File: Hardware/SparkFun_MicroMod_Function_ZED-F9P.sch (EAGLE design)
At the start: 51 parts, among them J2 MICROMOD_STANDARD, J3 QWIIC_RA, U1 EEPROM, U2 PCA9306DCUR, U3 U-BLOX_ZED-F9P, U4 74LVC541ABQ, U5 74LVC541ABQ, U6 SN74AUP1T04DCK

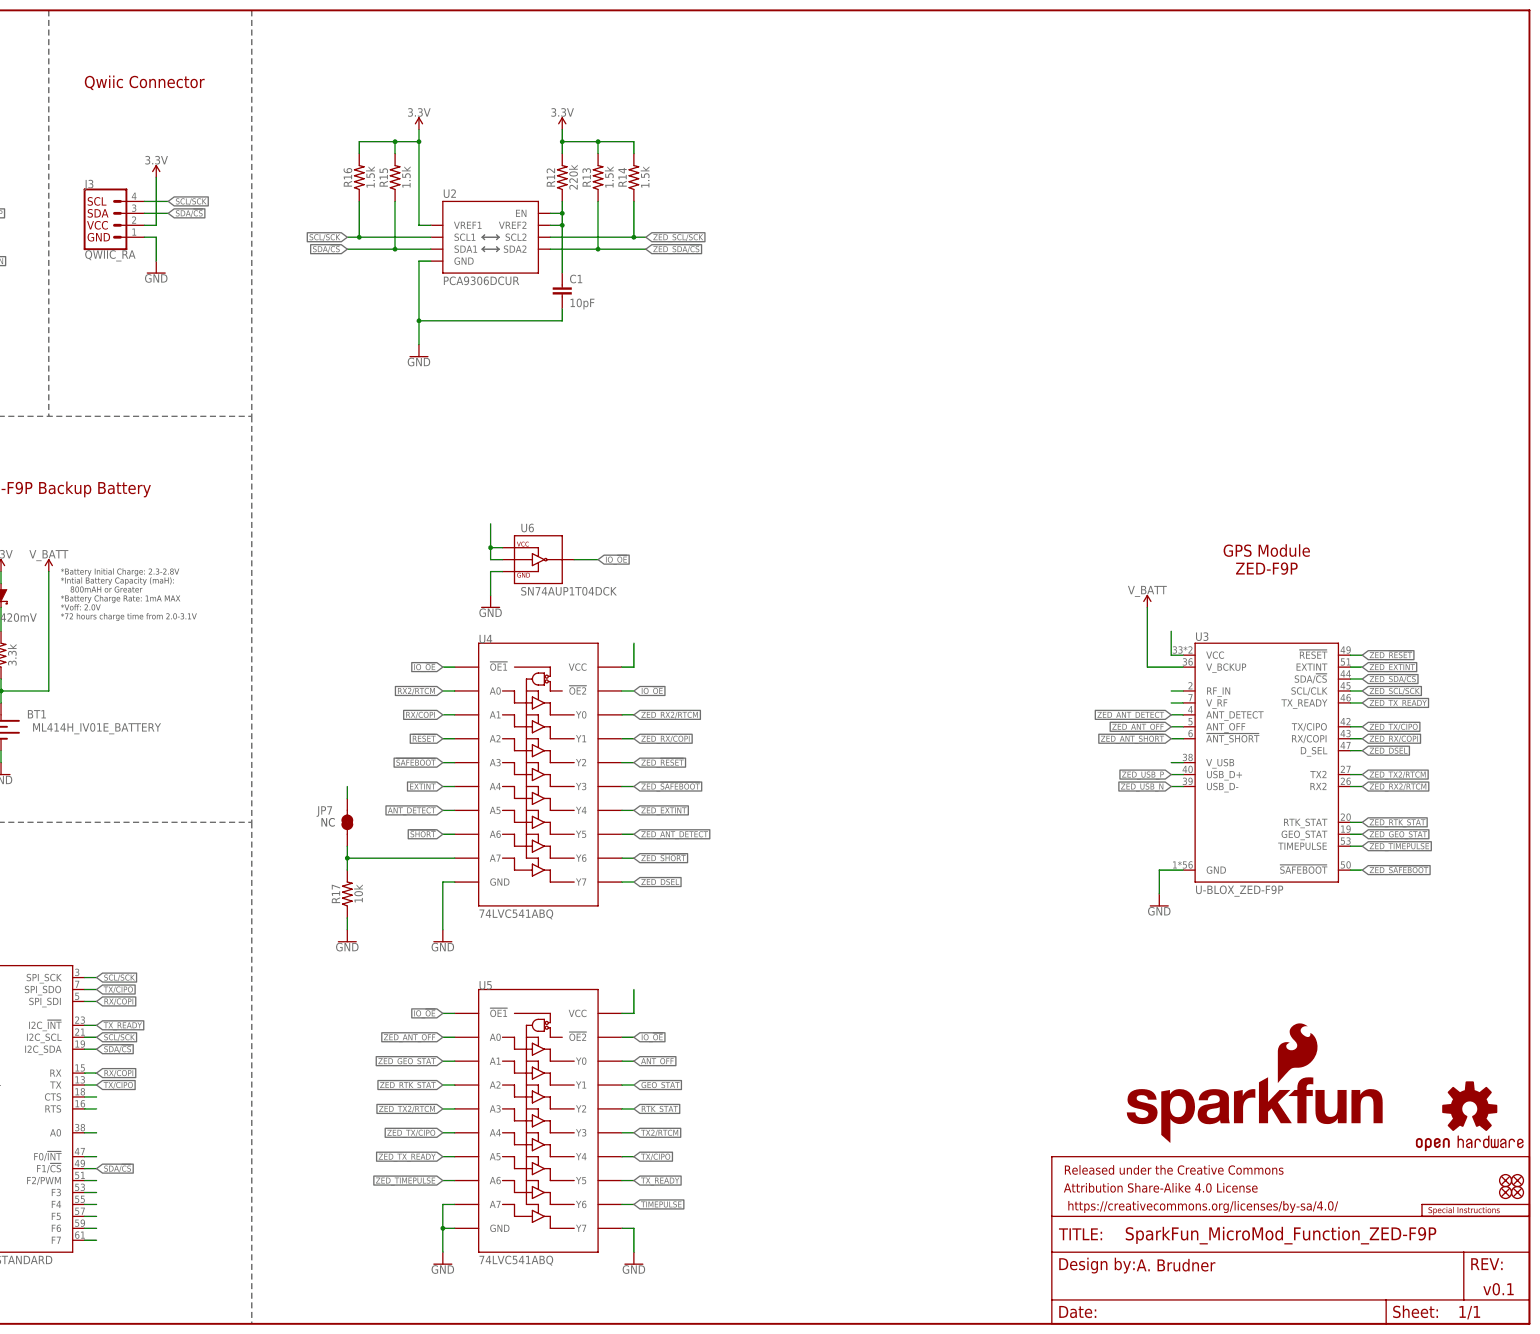
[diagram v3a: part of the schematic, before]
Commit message: Added I/O and passives. Changed net names.
Added passives surrounding IC's.
Modified names to be more descriptive.
Reorganized schematic for visual representation.
Added Descriptions of schematic symbols.
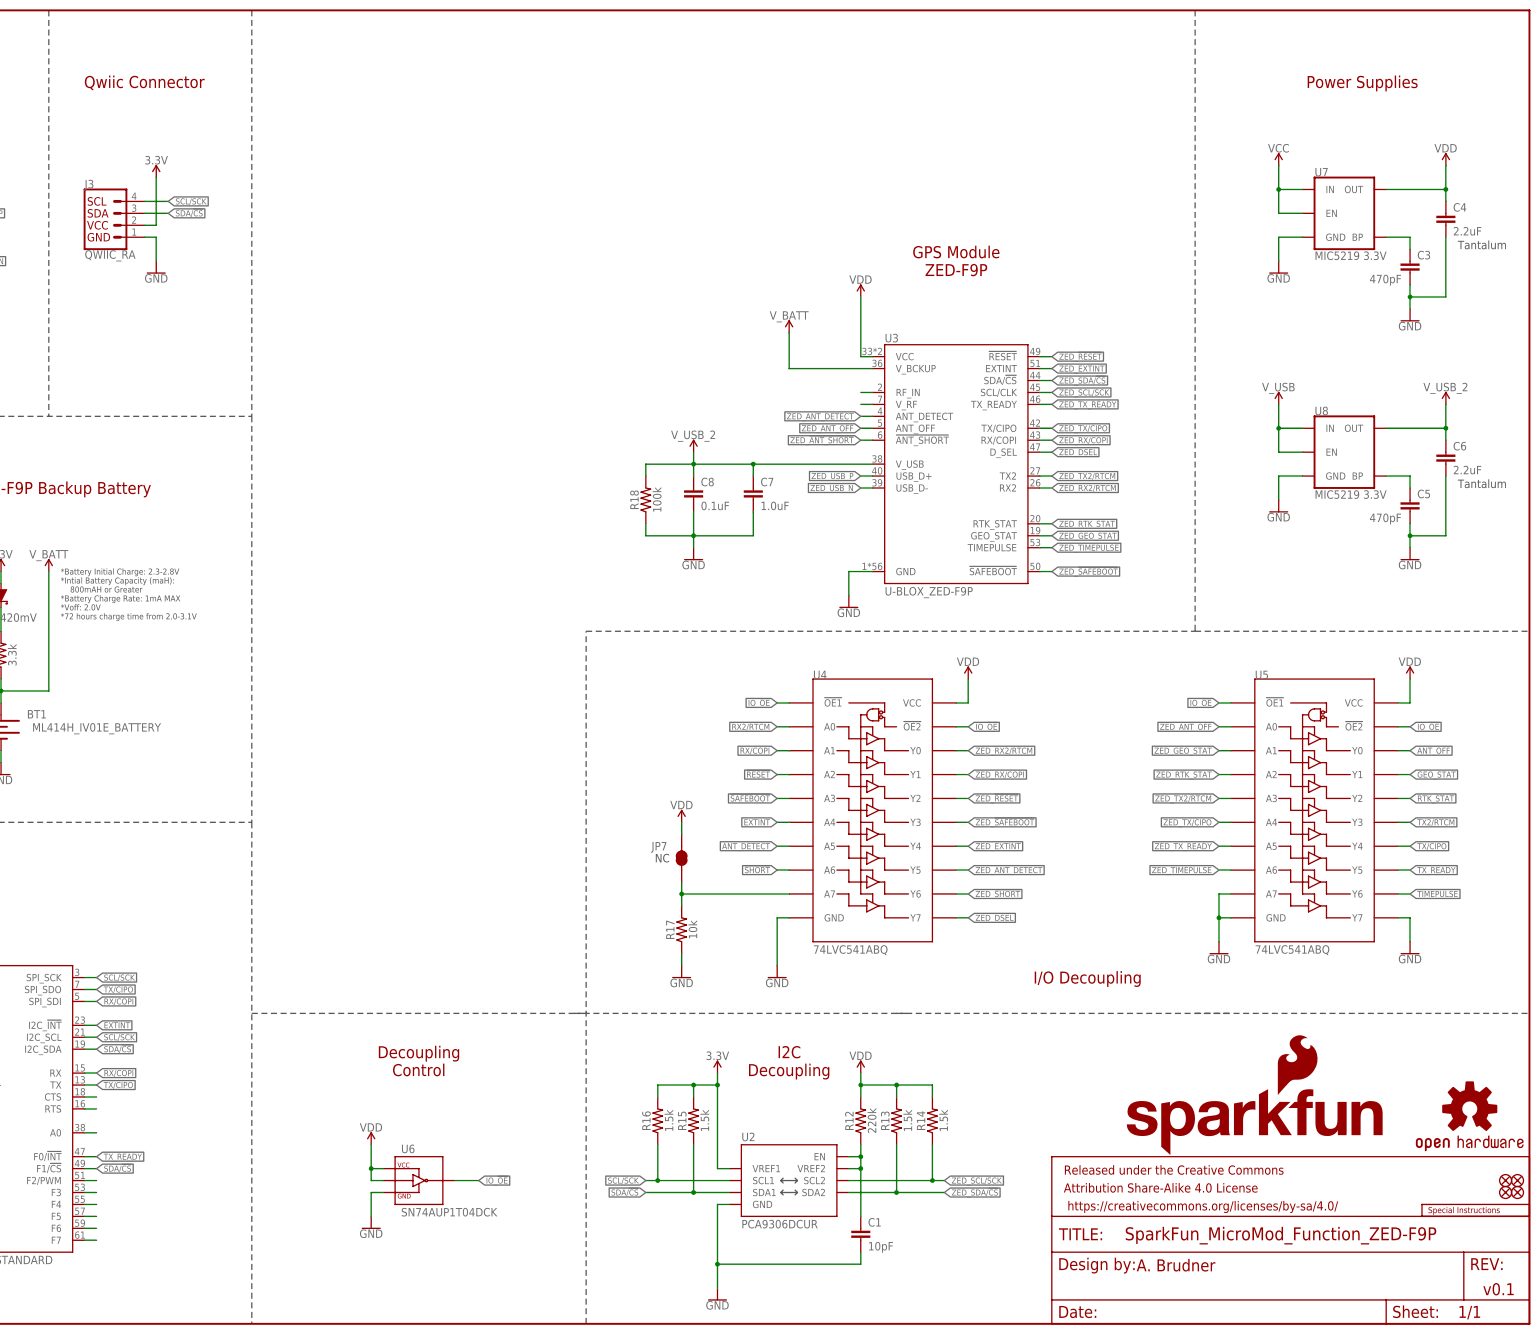
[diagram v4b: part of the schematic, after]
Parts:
- added C3, C5: 470pF, SparkFun-Capacitors:470PF-0603-50V-5%
- added C4, C6: 2.2uF, SparkFun-Capacitors:2.2UF-0603-10V-20%
- added C7: 1.0uF, SparkFun-Capacitors:1.0UF-0603-16V-10%
- added C8: 0.1uF, SparkFun-Capacitors:0.1UF-0402T-16V-10%
- added R18: 100k, SparkFun-Resistors:100KOHM-0603-1/10W-1%
- added U7, U8: MIC5219 3.3V, SparkFun-IC-Power:V_REG_MIC52193.3V
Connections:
- removed net N$16: JP7.2
- removed net N$19: J2.F0/!INT!
- removed net N$39: U4.VCC
- removed net N$42: U5.VCC
- removed net N$69: U3.V_USB
- removed net N$77: U3.VCC
- new net N$17: C3.1, U7.BP
- new net VDD: C4.1, JP7.2, R12.2, R13.2, R14.2, U3.VCC, U4.VCC, U5.VCC, U6.A, U6.VCC, U7.OUT
- new net V_USB_2: C6.1, C7.1, C8.1, R18.2, U3.V_USB, U8.OUT
- net 3.3V: no longer R12.2, R13.2, R14.2
- net EXTINT: now also J2.I2C_!INT!
- net GND: now also C3.2, C4.2, C5.2, C6.2, C7.2, C8.2, R18.1, U7.GND, U8.GND
- net N$14: now also C5.1, U8.BP; no longer U6.A, U6.VCC
- net TX_READY: now also J2.F0/!INT!; no longer J2.I2C_!INT!
- net VCC: now also U7.EN, U7.IN
- net V_USB: now also U8.EN, U8.IN
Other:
- note added: "Decoupling Control"
- note added: "I/O Decoupling"
- note added: "I2C Decoupling"
- note added: "Power Supplies"
- note added: "Tantalum"
- moved on the sheet: C1, JP7, R12, R13, R14, R15, R16, R17, U2, U3, U4, U5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

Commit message: Completed antenna supervisor. Started External Antenna Power.
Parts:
- removed U3: U-BLOX_ZED-F9P, MicroMod_Function_GNSS_ublox_ZED-F9P:U-BLOX_ZED-F9P
- added BYP, USB_EN: JUMPER-SMT_2_NO_SILK, SparkFun-Jumpers:JUMPER-SMT_2_NO_SILK
- added C10, C11, C14: 0.1uF, SparkFun-Capacitors:0.1UF-0402-16V-10%
- added C12: GRM0335C1H470JA01, MicroMod_Function_GNSS_ublox_ZED_F9P:GRM0335C1H470JA01
- added C13: 10nF, SparkFun-Capacitors:10NF-0402T-25V-10%-X7R-WE
- added C9: 0402YD104JAT2A, MicroMod_Function_GNSS_ublox_ZED_F9P:0402YD104JAT2A
- added D10, D9: 3A/10V/280mV, SparkFun-DiscreteSemi:DIODE-SCHOTTKY-BAT60A
- added D11, D12, D8: RED, SparkFun-LED:LED-RED0603
- added D13: PESD0402, SparkFun-DiscreteSemi:PESD0402
- added F1: 6V/2A, SparkFun-Fuses:PPTC_6V2A
- added FB1: BLM18AG102BH1D, MicroMod_Function_GNSS_ublox_ZED_F9P:BLM18AG102BH1D
- added J4: U.FL, SparkFun-RF:ANTENNA-SMA-GROUNDEDEDGE_SMA
- added JP10, JP8, JP9: JUMPER-SMT_2_NC_TRACE_SILK, SparkFun-Jumpers:JUMPER-SMT_2_NC_TRACE_SILK
- added JP11, JP12: JUMPER-SMT_3_2-NC_TRACE_SILK, SparkFun-Jumpers:JUMPER-SMT_3_2-NC_TRACE_SILK
- added L1, L2: LQW15ANR12J00D, MicroMod_Function_GNSS_ublox_ZED_F9P:LQW15ANR12J00D
- added Q1: DMP21D0UT, MicroMod_Function_GNSS_ublox_ZED_F9P:DMP21D0UT
- added Q2, Q3: 600mA/40V, SparkFun-DiscreteSemi:TRANS_PNP-MMBT4403
- added R19, R20, R21, R23: 1k, SparkFun-Resistors:1KOHM-0603-1/10W-1%
- added R22, R26: CRGP2010F10R, MicroMod_Function_GNSS_ublox_ZED_F9P:CRGP2010F10R
- added R24, R25: 100k, SparkFun-Resistors:100KOHM-0603-1/10W-1%
- added R27: 220, SparkFun-Resistors:220OHM-0603-1/10W-1%
- added R28: 2.2k, SparkFun-Resistors:2.2KOHM-0603-1/10W-1%
- added U$3: OPA344, SparkFun-IC-Amplifiers:OPA344
- added U9: 74LVC541ABQ, MicroMod_Function_GNSS_ublox_ZED_F9P:74LVC541ABQ
- JP7: value NC -> JUMPER-SMT_2_NO_SILK; device SparkFun-Jumpers:JUMPER-SMT_2_NC_TRACE_SILK -> SparkFun-Jumpers:JUMPER-SMT_2_NO_SILK
- R17: value 10k -> 100k; device SparkFun-Resistors:10KOHM-0603-1/10W-1% -> SparkFun-Resistors:100KOHM-0603-1/10W-1%
- U2: value PCA9306DCUR -> U-BLOX_ZED-F9P; device MicroMod_Function_GNSS_ublox_ZED-F9P:PCA9306DCUR -> MicroMod_Function_GNSS_ublox_ZED_F9P:U-BLOX_ZED-F9P
- U4: value 74LVC541ABQ -> SN74AUP1T04DCK; device MicroMod_Function_GNSS_ublox_ZED-F9P:74LVC541ABQ -> MicroMod_Function_GNSS_ublox_ZED_F9P:SN74AUP1T04DCK
- U5: value 74LVC541ABQ -> PCA9306DCUR; device MicroMod_Function_GNSS_ublox_ZED-F9P:74LVC541ABQ -> MicroMod_Function_GNSS_ublox_ZED_F9P:PCA9306DCUR
- U6: value SN74AUP1T04DCK -> 74LVC541ABQ; device MicroMod_Function_GNSS_ublox_ZED-F9P:SN74AUP1T04DCK -> MicroMod_Function_GNSS_ublox_ZED_F9P:74LVC541ABQ
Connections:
- removed net !SHORT!: U4.A6
- removed net N$73: U3.V_RF
- removed net N$74: U3.RF_IN
- removed net TIMEPULSE: U5.Y6
- removed net ZED_!ANT_SHORT!: U3.!ANT_SHORT!
- removed net ZED_!SHORT!: U4.Y6
- removed net ZED_TIMEPULSE: U3.TIMEPULSE, U5.A6
- new net ANT_!SHORT!: Q1.D, R22.2, R23.2, U6.A6
- new net GND2: JP10.2, JP2.2, JP3.2, JP4.1, JP5.1, JP6.1, JP8.2, JP9.2
- new net GND_RF: C13.2, C14.1, C3.2, C4.2, C5.2, C6.2, C7.2, C8.2, C9.2, D13.1, J4.GND, R18.1, R24.1, R28.1, U$3G2.P$V-, U2.GND
- new net N$15: JP8.1, R19.1
- new net N$16: D8.C, R19.2
- new net N$19: D10.A, USB_EN.2
- new net N$20: BYP.1, D10.C, D9.C, F1.1
- new net N$39: JP10.1, R21.1
- new net N$40: D12.C, R21.2
- new net N$41: C9.1, L2.2, Q3.C
- new net N$42: JP12.1, R14.2
- new net N$43: JP11.1, R15.2
- new net N$44: JP11.3, R16.2
- new net N$47: JP12.3, R13.2
- new net N$48: R23.1, R24.2, U$3G1.+IN
- new net N$49: C13.1, L1.2, R22.1, U$3G1.-IN
- new net N$50: Q2.B, Q3.E, R26.1
- new net N$51: Q2.C, Q3.B, R28.2
- new net N$52: Q2.E, R27.1
- new net N$53: FB1.2, R26.2, R27.2
- new net RF_IN: C12.2, U2.RF_IN
- new net SMA_RF_IN: C12.1, D13.2, J4.SIGNAL, L1.1, L2.1
- new net V_RF: C14.2, Q1.S, R25.1, U$3G2.P$V+, U2.V_RF
- new net ZED_ANT_!SHORT!: U2.!ANT_SHORT!, U6.Y6
- new net ZED_PPS: U2.TIMEPULSE, U9.A6
- net !RESET!: now also U6.A2; no longer U4.A2
- net !SAFEBOOT!: now also U6.A3; no longer U4.A3
- net 3.3V: now also JP11.2, U5.VREF1; no longer R15.2, R16.2, U2.VREF1
- net ANT_DETECT: now also U$3G1.OUT, U6.A5; no longer U4.A5
- net ANT_OFF: now also Q1.G, R25.2, U9.Y0; no longer U5.Y0
- net EXTINT: now also U6.A4; no longer U4.A4
- net GEO_STAT: now also U9.Y1; no longer U5.Y1
- net GND: now also C10.2, C11.2, JP7.1, U9.A7, U9.GND, U9.Y7; no longer C3.2, C4.2, C5.2, C6.2, C7.2, C8.2, JP2.2, JP3.2, JP4.1, JP5.1, JP6.1, R17.1, R18.1, U2.GND, U3.GND, U5.A7, U5.Y7
- net IO_!OE!: now also U4.Y, U6.!OE1!, U6.!OE2!, U9.!OE1!, U9.!OE2!; no longer U4.!OE1!, U4.!OE2!, U5.!OE1!, U5.!OE2!, U6.Y
- net N$12: now also U5.EN, U5.VREF2; no longer U2.EN, U2.VREF2
- net N$24: now also JP7.2, R17.1, U6.A7; no longer JP7.1, R17.2, U4.A7
- net N$26: now also JP9.1, R20.1; no longer J2.F6
- net N$30: now also D11.C, R20.2; no longer J2.F7
- net PPS: now also U9.Y6
- net RTK_STAT: now also U9.Y2; no longer U5.Y2
- net RX/COPI: now also U6.A1; no longer U4.A1
- net RX2/RTCM: now also J2.F7, U6.A0; no longer U4.A0
- net SCL/SCK: now also U5.SCL1; no longer U2.SCL1
- net SDA/!CS!: now also U5.SDA1; no longer U2.SDA1
- net TX/CIPO: now also U9.Y4; no longer U5.Y4
- net TX2/RTCM: now also J2.F6, U9.Y3; no longer U5.Y3
- net TX_READY: now also U9.Y5; no longer U5.Y5
- net VCC: now also BYP.2, F1.2; no longer J2.VCC
- net VDD: now also C10.1, C11.1, D11.A, JP12.2, R17.2, U2.VCC, U4.A, U8.EN, U9.VCC; no longer JP7.2, R13.2, R14.2, U3.VCC, U5.VCC, U6.A
- net VIN: now also D9.A, J2.VCC
- net V_BATT: now also U2.V_BCKUP; no longer U3.V_BCKUP
- net V_USB: now also D8.A, USB_EN.1; no longer U8.EN
- net V_USB_2: now also D12.A, U2.V_USB; no longer U3.V_USB
- net ZED_!RESET!: now also U2.!RESET!, U6.Y2; no longer U3.!RESET!, U4.Y2
- net ZED_!SAFEBOOT!: now also U2.!SAFEBOOT!, U6.Y3; no longer U3.!SAFEBOOT!, U4.Y3
- net ZED_ANT_DETECT: now also U2.ANT_DETECT, U6.Y5; no longer U3.ANT_DETECT, U4.Y5
- net ZED_ANT_OFF: now also U2.ANT_OFF, U9.A0; no longer U3.ANT_OFF, U5.A0
- net ZED_DSEL: now also U2.D_SEL, U6.Y7; no longer U3.D_SEL, U4.Y7
- net ZED_EXTINT: now also U2.EXTINT, U6.Y4; no longer U3.EXTINT, U4.Y4
- net ZED_GEO_STAT: now also U2.GEO_STAT, U9.A1; no longer U3.GEO_STAT, U5.A1
- net ZED_RTK_STAT: now also U2.RTK_STAT, U9.A2; no longer U3.RTK_STAT, U5.A2
- net ZED_RX/COPI: now also U2.RX/COPI, U6.Y1; no longer U3.RX/COPI, U4.Y1
- net ZED_RX2/RTCM: now also U2.RX2, U6.Y0; no longer U3.RX2, U4.Y0
- net ZED_SCL/SCK: now also U2.SCL/CLK, U5.SCL2; no longer U2.SCL2, U3.SCL/CLK
- net ZED_SDA/!CS!: now also U2.SDA/!CS!, U5.SDA2; no longer U2.SDA2, U3.SDA/!CS!
- net ZED_TX/CIPO: now also U2.TX/CIPO, U9.A4; no longer U3.TX/CIPO, U5.A4
- net ZED_TX2/RTCM: now also U2.TX2, U9.A3; no longer U3.TX2, U5.A3
- net ZED_TX_READY: now also U2.TX_READY, U9.A5; no longer U3.TX_READY, U5.A5
- net ZED_USB_N: no longer U3.USB_D-
- net ZED_USB_P: no longer U3.USB_D+
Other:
- note added: "Board thickness: 1.6mm"
- note added: "Calculated Impedance: 49.98 Ohm"
- note added: "Close to enable SPI."
- note added: "Close to enable USB power-up."
- note added: "Co-planar Calculation:"
- note added: "Copper Thickness (1oz): 1.4mil/0.035mm"
- note added: "Cut jumpers to remove I2C pullups from bus"
- note added: "Dielectric thickness: 0.18mm"
- note added: "Er: 4.6"
- note added: "NO"
- note added: "No clean process"
- note added: "Place capacitor as close as possible to module."
- note added: "Place diode close to connector."
- note added: "Polygon Isolation: .46mm"
- note added: "Power Selection"
- note added: "Pull ANT_OFF Low to use an external antenna supply."
- note added: "RECALCULATE"
- note added: "RF Trace Width: 0.35mm"
- note removed: "NC"
- moved on the sheet: C1, C2, C7, C8, D1, D2, D3, D4, D5, J2, J3, JP1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
